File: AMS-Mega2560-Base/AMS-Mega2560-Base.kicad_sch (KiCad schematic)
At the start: 28 parts, among them IC6 OPA2340PA, J1 RTD1, J2 RTD2, J3 Conn_01x08, J31 Conn_01x02, J32 Conn_01x02, J4 Sense1, J5 Sense2, J6 AdafruitUltimateGPS, J7 Conn_02x03_Odd_Even, P1 Power, P10 CONN_01X01, P11 CONN_01X01, P12 CONN_01X01, P13 CONN_01X01, P2 Analog, P3 Analog, P4 Digital, P5 PWM, P6 PWM, P7 Communication, P8 CONN_01X01, P9 CONN_01X01

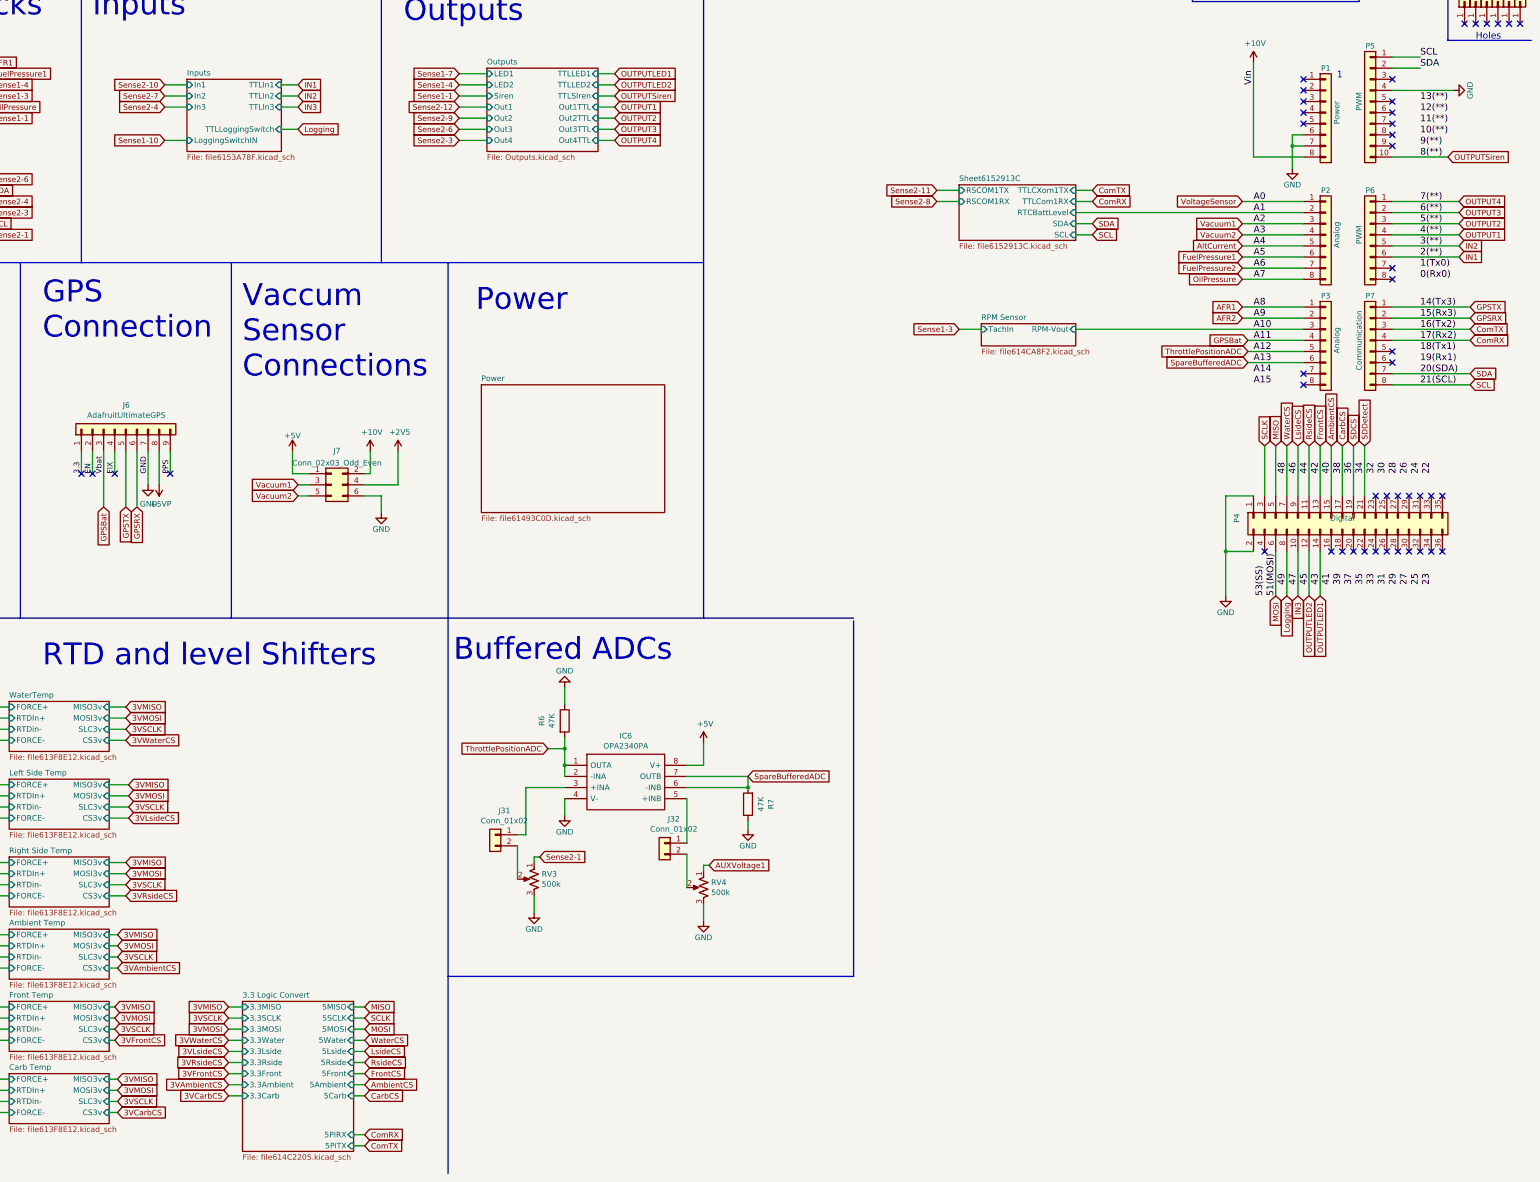
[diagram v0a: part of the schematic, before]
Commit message: cleared all of the ERC stuff need to go over some of the power stuff for this before finishing routing.
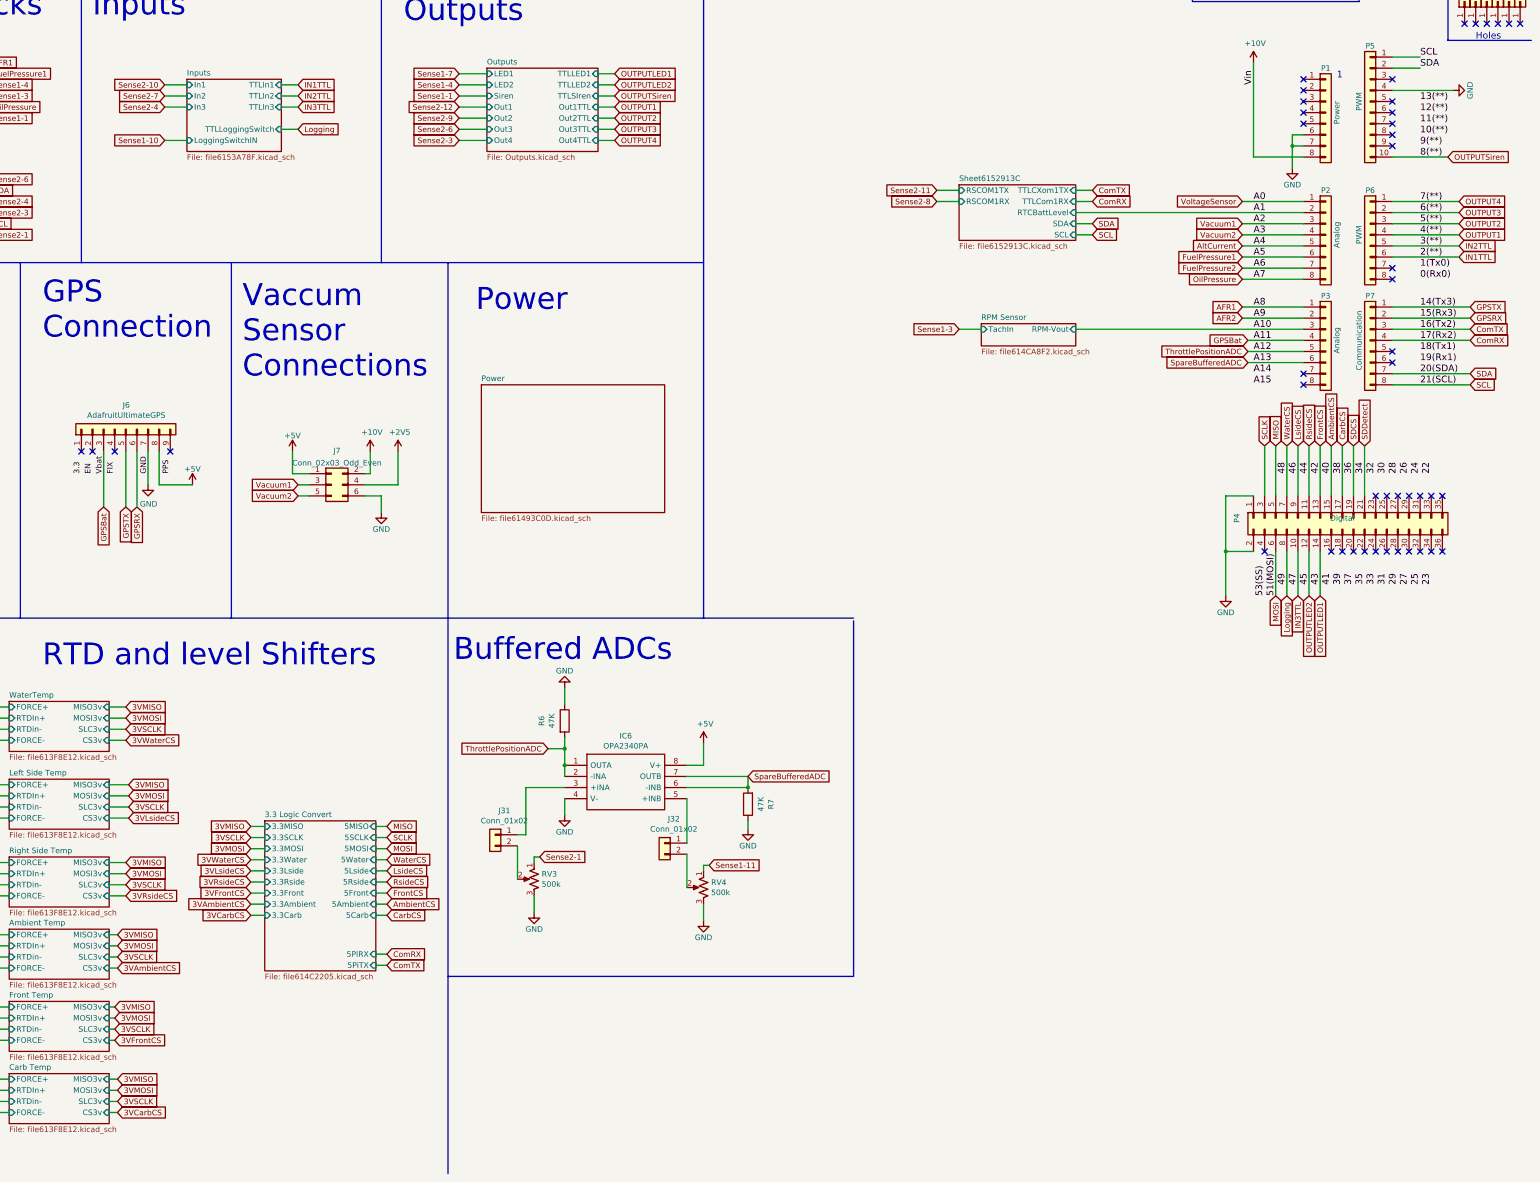
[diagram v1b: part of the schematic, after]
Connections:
- net +5VP is gone; now on net +5V: J6.8 (Pin_8)
- net AUXVoltage1 is gone; now on net Sense1-11: RV4.1
- net 3.3: no longer J6.1 (Pin_1)
- net EN: no longer J6.2 (Pin_2)
- net FIX: no longer J6.4 (Pin_4)
- net PPS: no longer J6.9 (Pin_9)
- net IN1 renamed IN1TTL
- net IN2 renamed IN2TTL
- net IN3 renamed IN3TTL

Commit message: pushing this change to the repo need to vet some schematics
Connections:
- net Sense1-10: now also RV3.1
- net Sense2-1: no longer RV3.1
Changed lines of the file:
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@@
     (stroke (width 0) (type default) (color 0 0 0 0))
   )
-  (wire (pts (xy 177.8 207.01) (xy 177.8 196.215))
+  (wire (pts (xy 182.88 212.725) (xy 179.705 212.725))
     (stroke (width 0) (type default) (color 0 0 0 0))
   )
-  (wire (pts (xy 95.25 48.26) (xy 100.33 48.26))
+  (wire (pts (xy 177.8 207.01) (xy 177.8 196.215))
     (stroke (width 0) (type default) (color 0 0 0 0))
   )
@@
     (stroke (width 0) (type default) (color 0 0 0 0))
   )
-  (wire (pts (xy 179.705 213.36) (xy 179.705 212.09))
-    (stroke (width 0) (type default) (color 0 0 0 0))
-  )
   (wire (pts (xy 148.59 127) (xy 140.97 127))
     (stroke (width 0) (type default) (color 0 0 0 0))
@@
     (stroke (width 0) (type default) (color 0 0 0 0))
   )
-  (wire (pts (xy 179.705 212.09) (xy 180.975 212.09))
-    (stroke (width 0) (type default) (color 0 0 0 0))
-  )
   (wire (pts (xy 128.27 124.46) (xy 124.46 124.46))
     (stroke (width 0) (type default) (color 0 0 0 0))
@@
     (stroke (width 0) (type default) (color 0 0 0 0))
   )
+  (wire (pts (xy 179.705 212.725) (xy 179.705 213.36))
+    (stroke (width 0) (type default) (color 0 0 0 0))
+  )
   (wire (pts (xy 82.55 200.66) (xy 86.995 200.66))
     (stroke (width 0) (type default) (color 0 0 0 0))
@@
     (stroke (width 0) (type default) (color 0 0 0 0))
   )
+  (wire (pts (xy 95.25 48.26) (xy 100.33 48.26))
+    (stroke (width 0) (type default) (color 0 0 0 0))
+  )
   (wire (pts (xy 49.53 198.12) (xy 33.02 198.12))
     (stroke (width 0) (type default) (color 0 0 0 0))
@@
     )
   )
-  (global_label "Sense1-10" (shape input) (at 95.25 48.26 180) (fields_autoplaced)
-    (effects (font (size 1.27 1.27)) (justify right))
-    (property "Intersheet References" "${INTERSHEET_REFS}" (id 0) (at 82.161 48.1806 0)
-      (effects (font (size 1.27 1.27)) (justify right) hide)
+  (global_label "Sense1-10" (shape input) (at 182.88 212.725 0) (fields_autoplaced)
+    (effects (font (size 1.27 1.27)) (justify left))
+    (property "Intersheet References" "${INTERSHEET_REFS}" (id 0) (at 195.969 212.6456 0)
+      (effects (font (size 1.27 1.27)) (justify left) hide)
     )
   )
@@
     )
   )
-  (global_label "Sense2-1" (shape input) (at 180.975 212.09 0) (fields_autoplaced)
-    (effects (font (size 1.27 1.27)) (justify left))
-    (property "Intersheet References" "${INTERSHEET_REFS}" (id 0) (at 192.8544 212.0106 0)
-      (effects (font (size 1.27 1.27)) (justify left) hide)
+  (global_label "Sense2-1" (shape input) (at 95.25 48.26 180) (fields_autoplaced)
+    (effects (font (size 1.27 1.27)) (justify right))
+    (property "Intersheet References" "${INTERSHEET_REFS}" (id 0) (at 83.3706 48.1806 0)
+      (effects (font (size 1.27 1.27)) (justify right) hide)
     )
   )
@@
       (reference "Q21") (unit 1) (value "IRF9Z34NPBF") (footprint "SamacSys_Parts:TO254P469X1042X1967-3P")
     )
-    (path "/00000000-0000-0000-0000-000061493c0e/14fa351f-a44c-4cb9-86de-bc4ce1266c39"
-      (reference "Q22") (unit 1) (value "BD140") (footprint "Package_TO_SOT_THT:TO-126-3_Vertical")
+    (path "/00000000-0000-0000-0000-000061493c0e/54b9aef8-b50a-46a4-bd39-fa76fe97d610"
+      (reference "Q22") (unit 1) (value "IRF9610PBF-BE3") (footprint "TO254P465X1024X2050-3P")
     )
     (path "/00000000-0000-0000-0000-000061493c0e/26286b82-8e1d-44de-8c30-eae394d0f76a"
@@
       (reference "R63") (unit 1) (value "1M") (footprint "Resistor_THT:R_Axial_DIN0207_L6.3mm_D2.5mm_P2.54mm_Vertical")
     )
-    (path "/00000000-0000-0000-0000-00006152913d/98dbeacd-eda1-4446-87dd-ddc62165f2c4"
-      (reference "R64") (unit 1) (value "4.7K") (footprint "Resistor_THT:R_Axial_DIN0207_L6.3mm_D2.5mm_P2.54mm_Vertical")
-    )
     (path "/00000000-0000-0000-0000-0000614ca8f3/00000000-0000-0000-0000-0000614e2c3c"

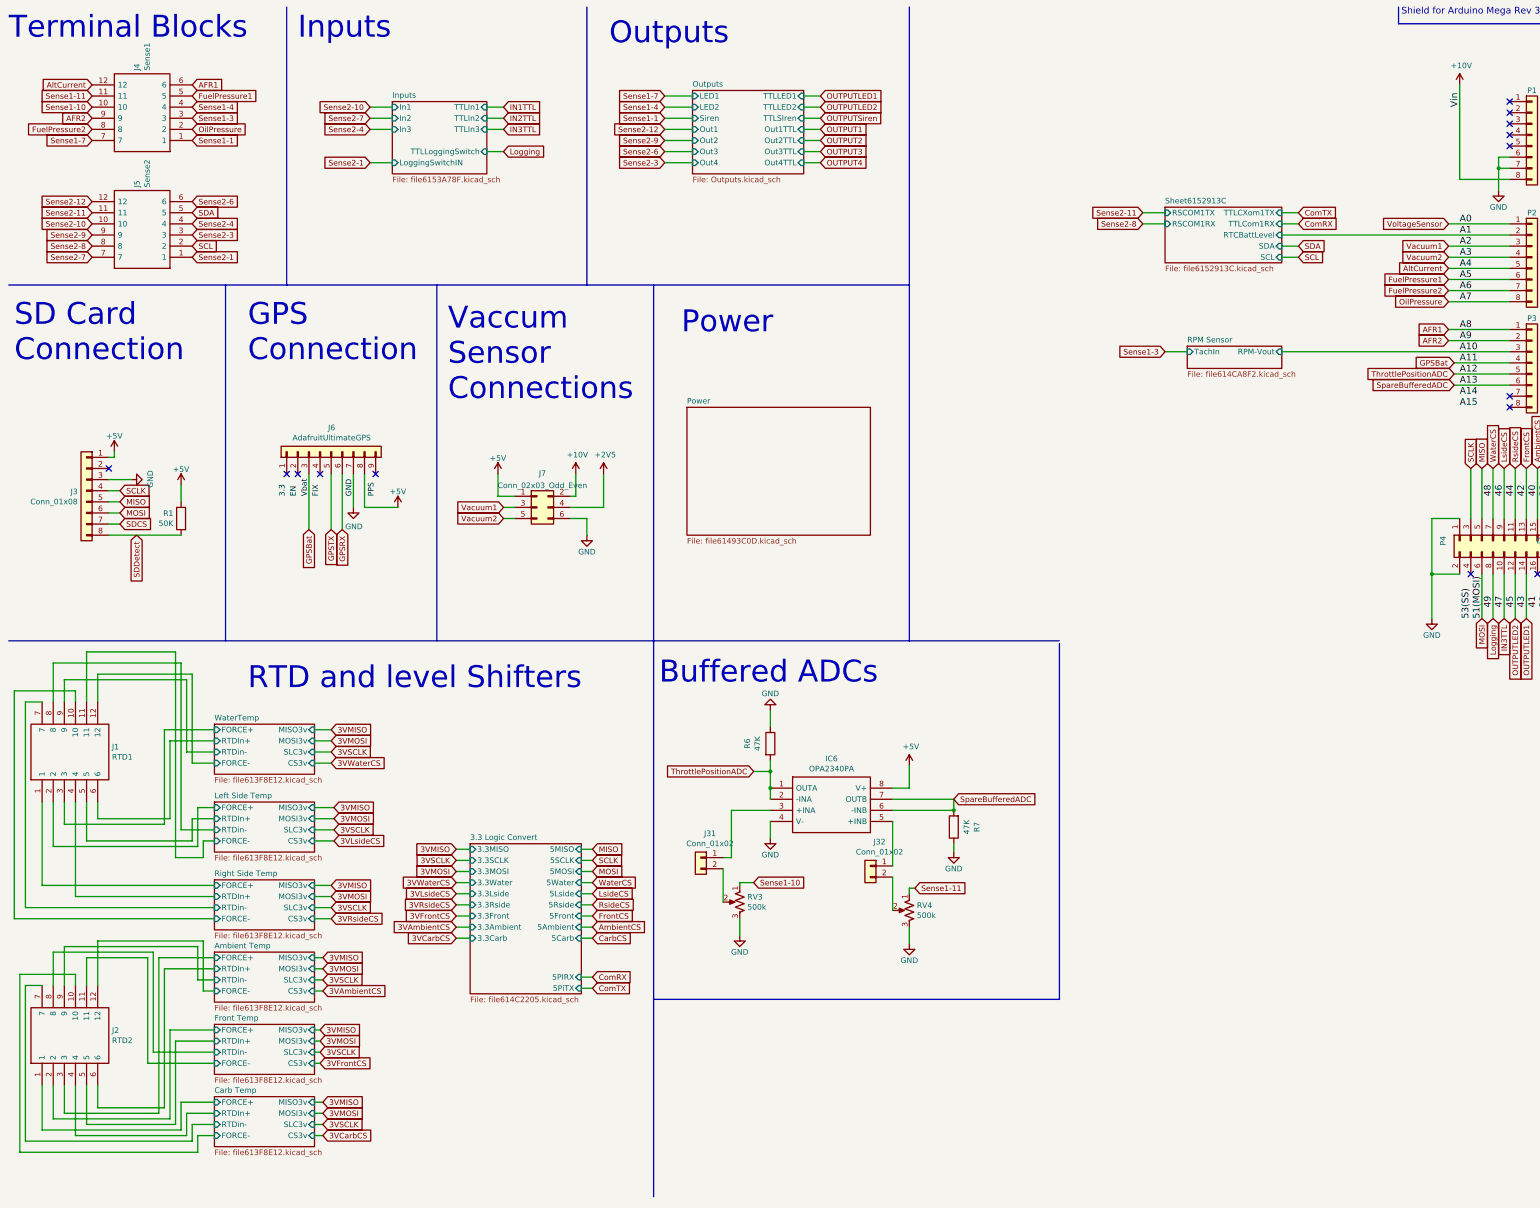
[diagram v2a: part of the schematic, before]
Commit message: adding some fixes for the RPM sensor and trying to fit everything on the board. WIp for FW
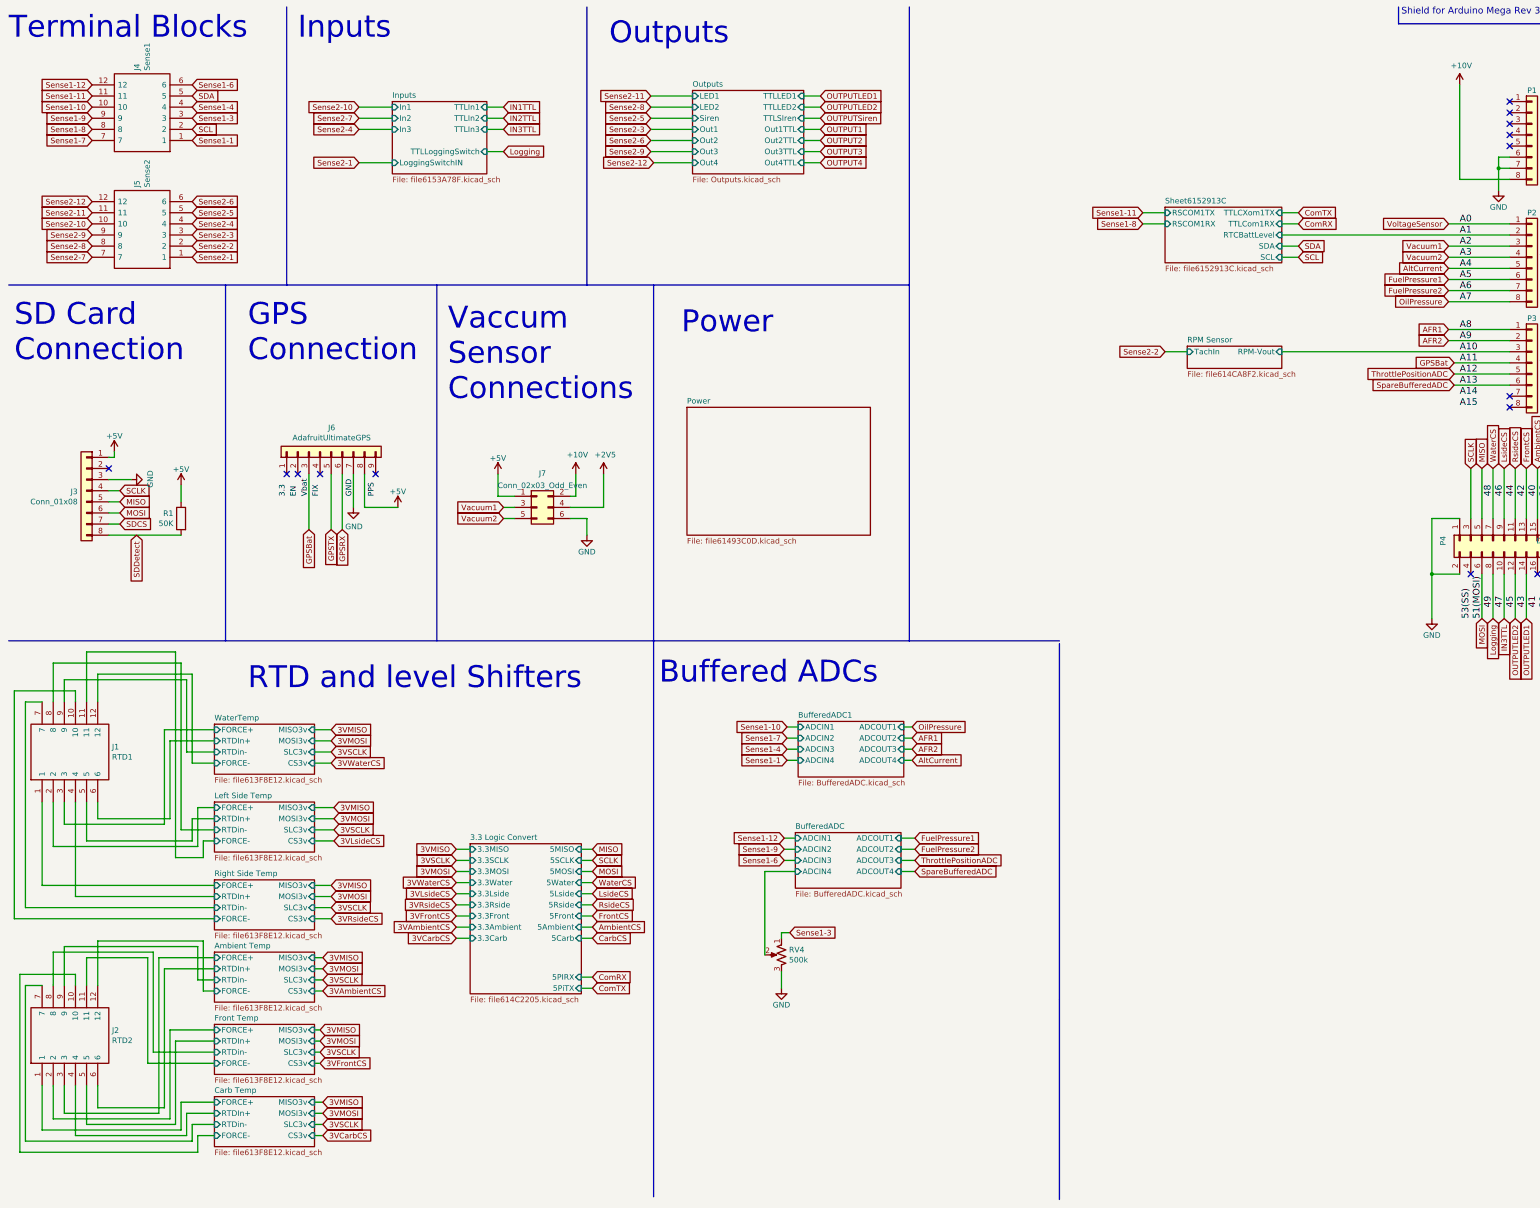
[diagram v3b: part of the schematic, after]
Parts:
- removed IC6: OPA2340PA, SamacSys_Parts:DIP794W53P254L959H508Q8N, symbol SamacSys_Parts:OPA2340PA
- removed J31, J32: Conn_01x02, Connector_PinHeader_2.54mm:PinHeader_1x02_P2.54mm_Vertical, symbol Connector_Generic:Conn_01x02
- removed R6, R7: 47K, Resistor_THT:R_Axial_DIN0207_L6.3mm_D2.5mm_P2.54mm_Vertical, symbol Device:R
- removed RV3: 500k, Potentiometer_THT:Potentiometer_Bourns_3296W_Vertical, symbol Device:R_POT_US
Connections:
- net AFR1: no longer J4.6
- net AFR2: no longer J4.9
- net AltCurrent: no longer J4.12
- net FuelPressure1: no longer J4.5
- net FuelPressure2: no longer J4.8
- net OilPressure: no longer J4.2
- net SCL: now also J4.2; no longer J5.2
- net SDA: now also J4.5; no longer J5.5
- net Sense1-11: no longer RV4.1
- net Sense1-3: now also RV4.1
- net BufferedADC/ADCIN4: now reaches RV4.2
- new net Sense1-12: J4.12
- new net Sense1-6: J4.6
- new net Sense1-8: J4.8
- new net Sense1-9: J4.9
- new net Sense2-2: J5.2
- new net Sense2-5: J5.5
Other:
- added sheet BufferedADC (BufferedADC.kicad_sch)
- added sheet BufferedADC1 (BufferedADC.kicad_sch)
- moved on the sheet: RV4
